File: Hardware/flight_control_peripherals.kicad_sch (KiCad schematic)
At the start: 16 parts, among them J2 DM3AT-SF-PEJM5, J5 Conn_02x10_Odd_Even, J6 Conn_01x10, J7 Conn_01x04, J8 Conn_01x04, U13 W25N01GVZEIG_TR, U14 24CW1280T-I/OT, U15 PCA9685PW_118

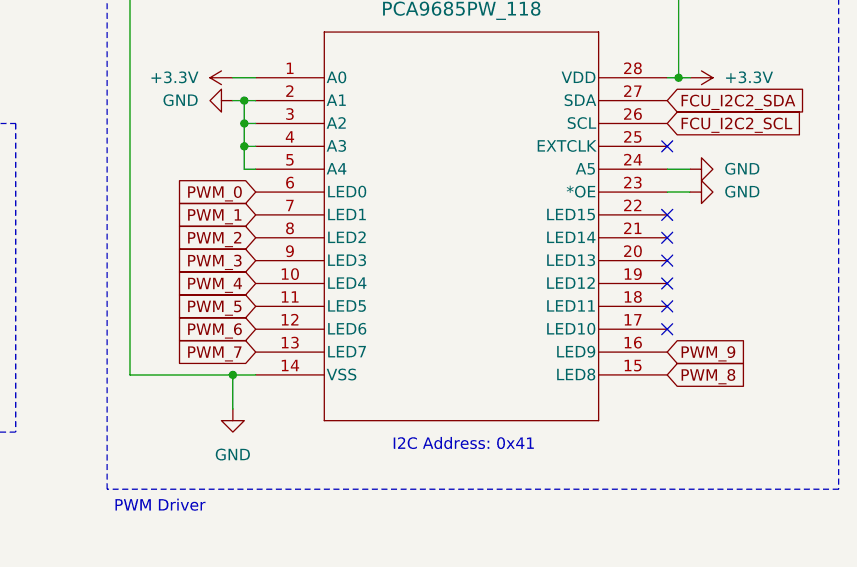
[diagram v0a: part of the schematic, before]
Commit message: fill zones done, layout reformulation because of 5v, power supply power traces done
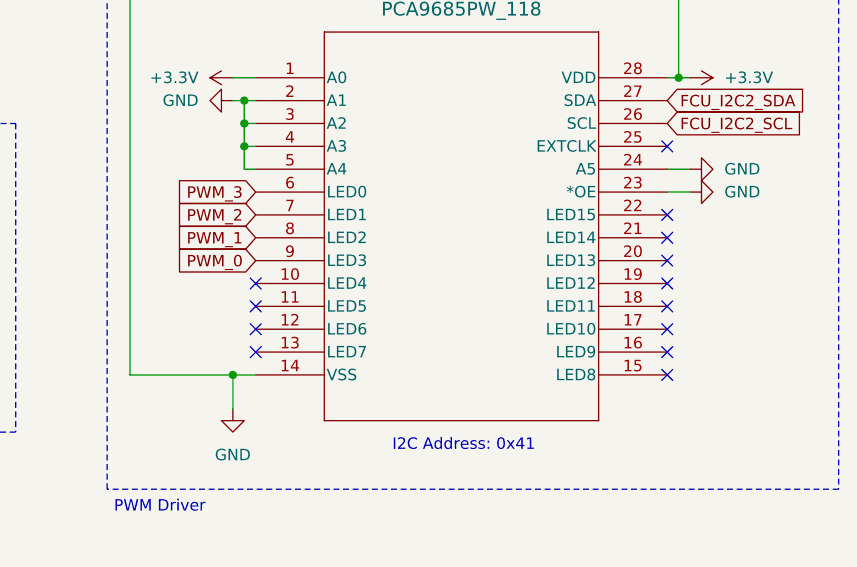
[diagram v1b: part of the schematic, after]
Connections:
- net PWM_0: now also U15.9 (LED3); no longer U15.6 (LED0)
- net PWM_1: now also U15.8 (LED2); no longer U15.7 (LED1)
- net PWM_2: now also U15.7 (LED1); no longer U15.8 (LED2)
- net PWM_3: now also U15.6 (LED0); no longer U15.9 (LED3)
- net PWM_4: no longer names the net of U15.10 (LED4)
- net PWM_5: no longer names the net of U15.11 (LED5)
- net PWM_6: no longer names the net of U15.12 (LED6)
- net PWM_7: no longer names the net of U15.13 (LED7)
- net PWM_8: no longer names the net of U15.15 (LED8)
- net PWM_9: no longer names the net of U15.16 (LED9)
- no-connect marks 12 -> 18
